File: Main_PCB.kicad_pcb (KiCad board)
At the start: 0 parts

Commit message: added battery holder and swd programming port
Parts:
- added A1: Arduino_UNO_R3, Module:Arduino_UNO_R3, F.Cu at (129.0, 71.5)
- added C3: 4pF, Capacitor_SMD:C_0603_1608Metric_Pad1.08x0.95mm_HandSolder, F.Cu at (96.1, 138.8)
- added C4: 4pF, Capacitor_SMD:C_0603_1608Metric_Pad1.08x0.95mm_HandSolder, F.Cu at (110.6, 124.3)
- added F1: Fuse, Fuse:Fuse_0603_1608Metric_Pad1.05x0.95mm_HandSolder, F.Cu at (208.7, 69.4)
- added JP1: 20021521-00010T1LF, 20021521-00010T1LF:20021521-00010T1LF, F.Cu at (205.5, 144.0)
- added U3: Dual_AA, Dual_AA:Dual_AA, F.Cu at (237.0, 73.5)
- added U4: STM32L476RGTx, Package_QFP:LQFP-64_10x10mm_P0.5mm, F.Cu at (150.5, 95.0)
- added Y1: 32.768, Crystal:Crystal_SMD_3215-2Pin_3.2x1.5mm, F.Cu at (110.9, 136.0)
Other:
- copper layers 0 -> 2

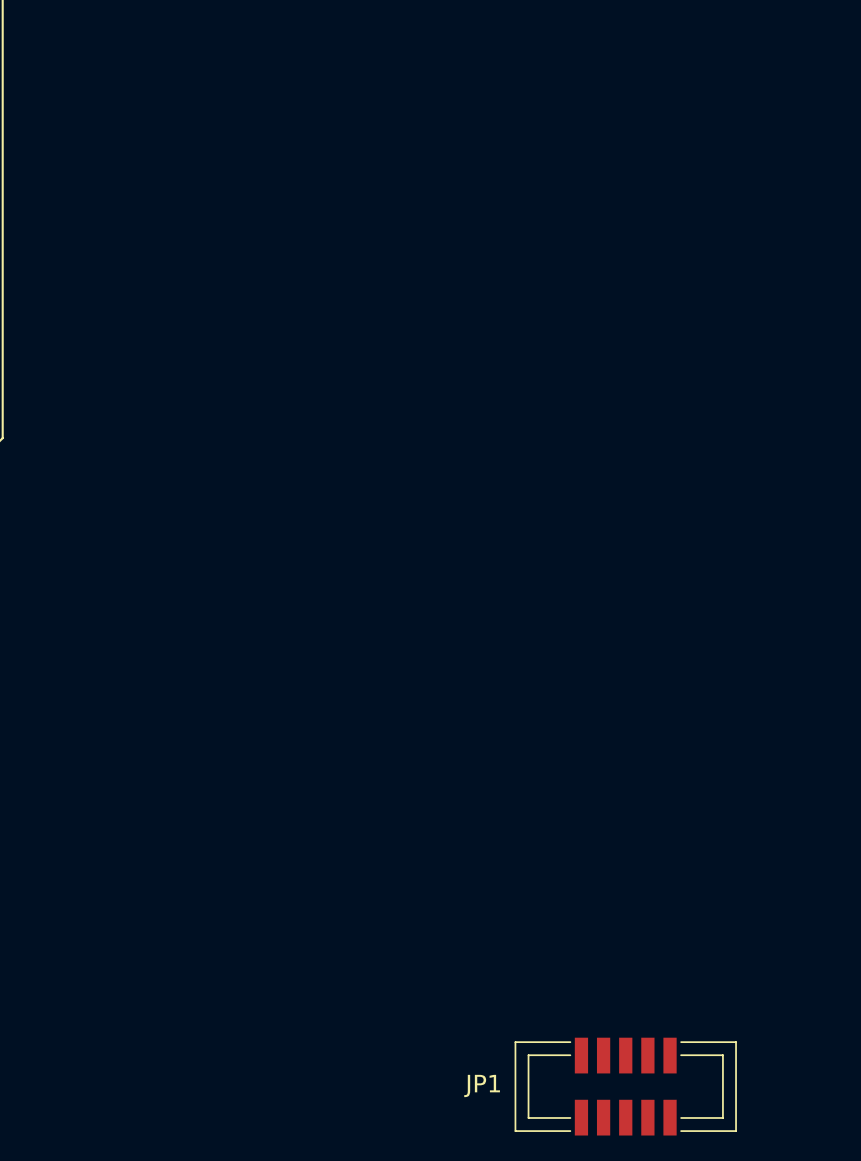
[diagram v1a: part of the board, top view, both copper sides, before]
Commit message: assigned footprints
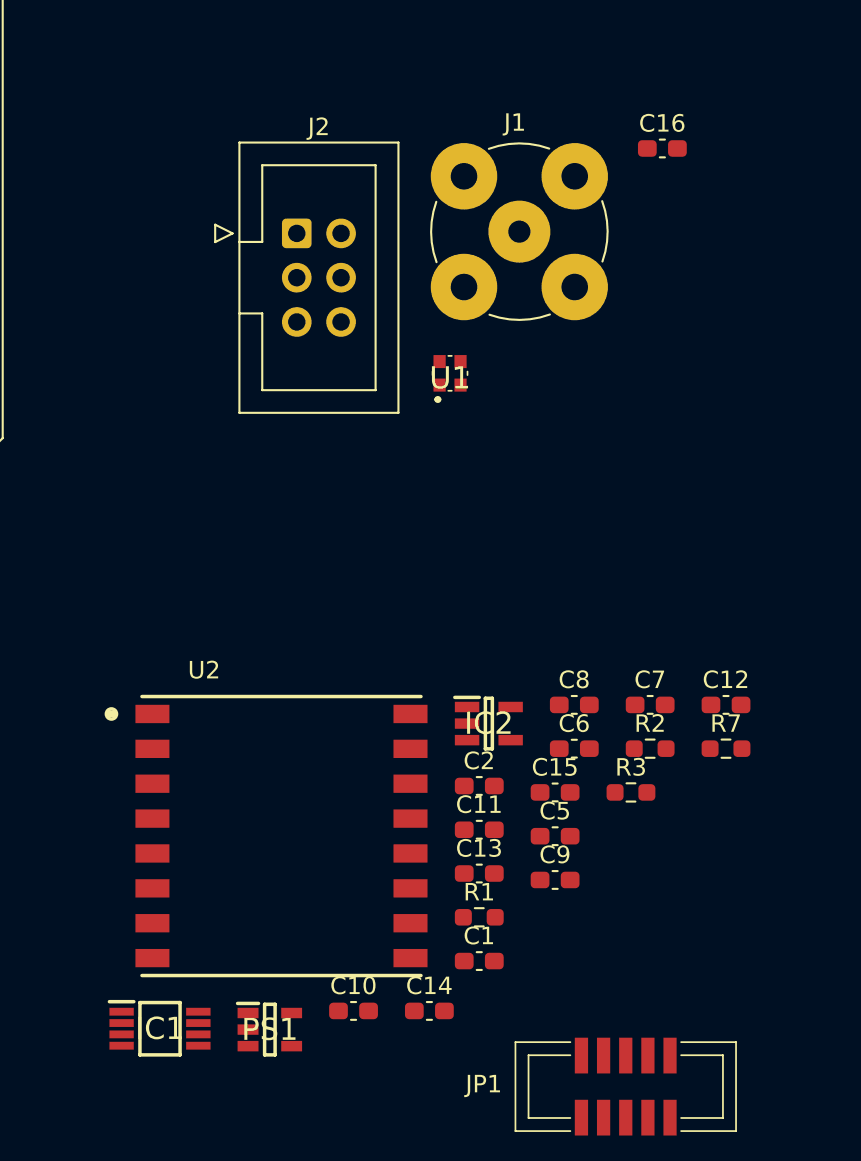
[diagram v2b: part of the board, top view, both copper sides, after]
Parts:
- added C1: 100nF, Capacitor_SMD:C_0603_1608Metric_Pad1.08x0.95mm_HandSolder, F.Cu at (197.1, 136.8)
- added C10: 100nF, Capacitor_SMD:C_0603_1608Metric_Pad1.08x0.95mm_HandSolder, F.Cu at (189.9, 139.7)
- added C11: 100nF, Capacitor_SMD:C_0603_1608Metric_Pad1.08x0.95mm_HandSolder, F.Cu at (197.1, 129.3)
- added C12: 100nF, Capacitor_SMD:C_0603_1608Metric_Pad1.08x0.95mm_HandSolder, F.Cu at (211.2, 122.1)
- added C13: 100nF, Capacitor_SMD:C_0603_1608Metric_Pad1.08x0.95mm_HandSolder, F.Cu at (197.1, 131.8)
- added C14: 100nF, Capacitor_SMD:C_0603_1608Metric_Pad1.08x0.95mm_HandSolder, F.Cu at (194.2, 139.7)
- added C15: 100nF, Capacitor_SMD:C_0603_1608Metric_Pad1.08x0.95mm_HandSolder, F.Cu at (201.4, 127.1)
- added C16: 100nF, Capacitor_SMD:C_0603_1608Metric_Pad1.08x0.95mm_HandSolder, F.Cu at (207.6, 90.2)
- added C2: 100nF, Capacitor_SMD:C_0603_1608Metric_Pad1.08x0.95mm_HandSolder, F.Cu at (197.1, 126.8)
- added C5: 100nF, Capacitor_SMD:C_0603_1608Metric_Pad1.08x0.95mm_HandSolder, F.Cu at (201.4, 129.6)
- added C6: 100nF, Capacitor_SMD:C_0603_1608Metric_Pad1.08x0.95mm_HandSolder, F.Cu at (202.6, 124.6)
- added C7: 100nF, Capacitor_SMD:C_0603_1608Metric_Pad1.08x0.95mm_HandSolder, F.Cu at (206.9, 122.1)
- added C8: 100nF, Capacitor_SMD:C_0603_1608Metric_Pad1.08x0.95mm_HandSolder, F.Cu at (202.6, 122.1)
- added C9: 100nF, Capacitor_SMD:C_0603_1608Metric_Pad1.08x0.95mm_HandSolder, F.Cu at (201.4, 132.2)
- added IC1: TCN75AVUA713-VAO, TCN75AVUA713-VAO:SOP65P490X110-8N, F.Cu at (178.8, 140.7)
- added IC2: 24AA64T-I_OT, 24AA64T-I_OT:SOT95P270X145-5N, F.Cu at (197.7, 123.2)
- added J1: Conn_Coaxial, Connector_Coaxial:BNC_TEConnectivity_1478204_Vertical, F.Cu at (199.4, 95.0)
- added J2: Conn_02x03_Odd_Even, Connector_IDC:IDC-Header_2x03_P2.54mm_Vertical, F.Cu at (186.6, 95.1)
- added PS1: S-1318B33-M5T1U4, S-1318B33:SOT95P275X130-5N, F.Cu at (185.1, 140.7)
- added R1: 0R, Resistor_SMD:R_0603_1608Metric_Pad0.98x0.95mm_HandSolder, F.Cu at (197.1, 134.3)
- added R2: 0R, Resistor_SMD:R_0603_1608Metric_Pad0.98x0.95mm_HandSolder, F.Cu at (206.9, 124.6)
- added R3: 4.7KR, Resistor_SMD:R_0603_1608Metric_Pad0.98x0.95mm_HandSolder, F.Cu at (205.8, 127.1)
- added R7: 10K, Resistor_SMD:R_0603_1608Metric_Pad0.98x0.95mm_HandSolder, F.Cu at (211.2, 124.6)
- added U1: LTR-329ALS-01, LTR-329ALS:LTR329ALS01, F.Cu at (195.4, 103.4)
- added U2: RFM95W-868S2, RFM95W-868S2:XCVR_RFM95W-868S2, F.Cu at (185.8, 129.6)

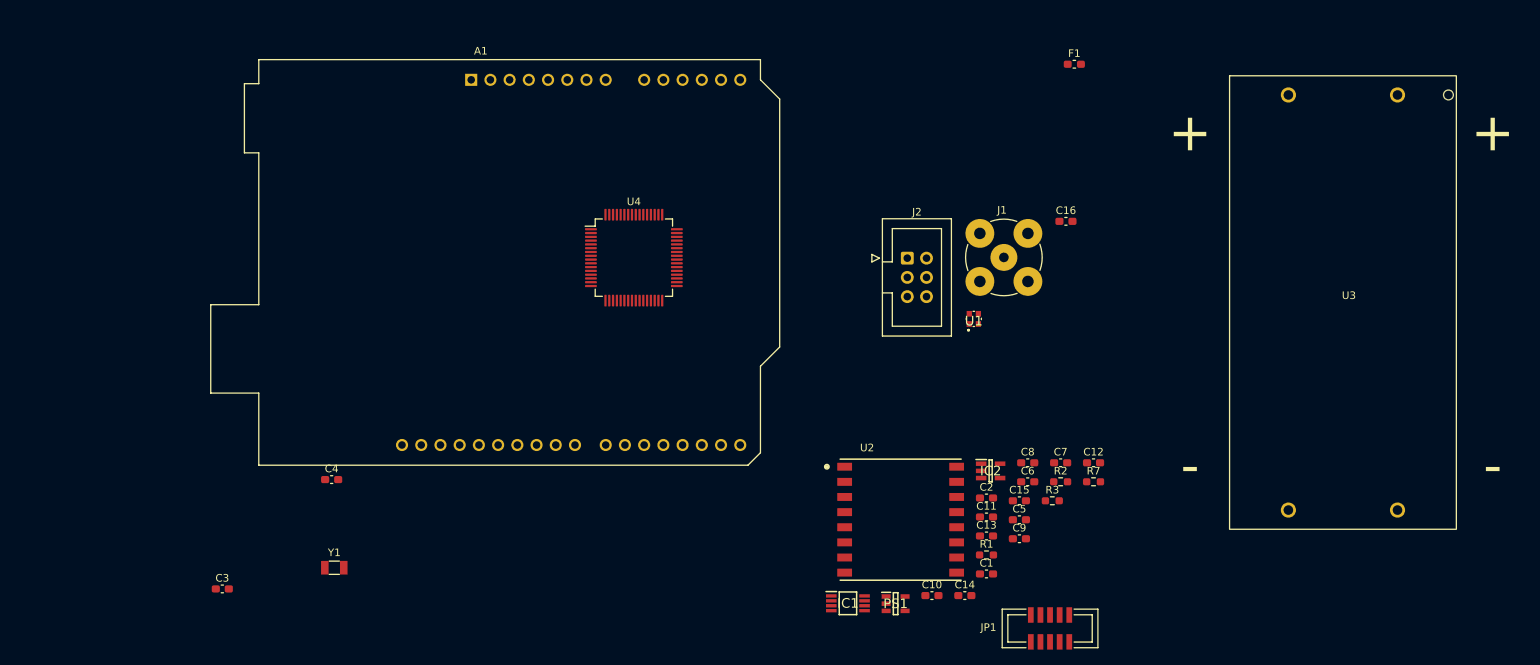
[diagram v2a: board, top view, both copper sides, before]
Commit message: did alot of the routing and pcb layout
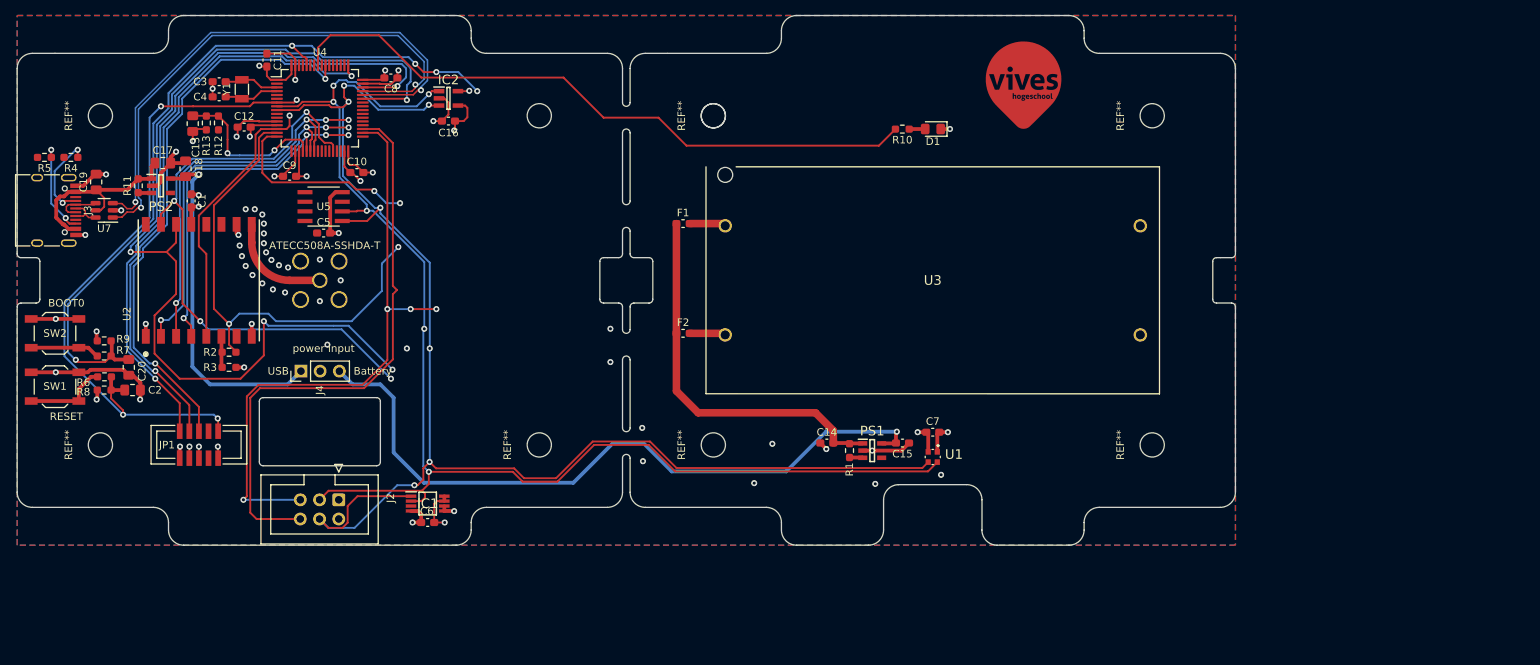
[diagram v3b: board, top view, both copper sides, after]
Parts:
- removed A1: Arduino_UNO_R3, Module:Arduino_UNO_R3
- added ?: , , F.Cu at (161.0, 76.2)
- added C17: 100nF, Capacitor_SMD:C_0805_2012Metric_Pad1.18x1.45mm_HandSolder, F.Cu at (88.2, 82.5)
- added C18: 100nF, Capacitor_SMD:C_0805_2012Metric_Pad1.18x1.45mm_HandSolder, F.Cu at (91.2, 83.2)
- added C19: 100nF, Capacitor_SMD:C_0805_2012Metric_Pad1.18x1.45mm_HandSolder, F.Cu at (79.4, 85.0)
- added C20: 100nF, Capacitor_SMD:C_0805_2012Metric_Pad1.18x1.45mm_HandSolder, F.Cu at (83.8, 109.5)
- added D1: LED, LED_SMD:LED_0805_2012Metric_Pad1.15x1.40mm_HandSolder, F.Cu at (190.0, 78.0)
- added F2: Fuse, Fuse:Fuse_0603_1608Metric_Pad1.05x0.95mm_HandSolder, F.Cu at (157.0, 105.0)
- added G***: LOGO, logo's:VIVES_LOGO_10MM, F.Cu at (202.0, 73.0)
- added J3: USB_C_Receptacle_USB2.0, Connector_USB:USB_C_Receptacle_HRO_TYPE-C-31-M-12, F.Cu at (72.7, 88.8)
- added J4: Conn_01x03_Male, Connector_PinHeader_2.54mm:PinHeader_1x03_P2.54mm_Vertical, F.Cu at (106.5, 110.0)
- added PS2: S-1318B33-M5T1U4, S-1318B33:SOT95P275X130-5N, F.Cu at (88.0, 85.5)
- added R10: 360R, Resistor_SMD:R_0603_1608Metric_Pad0.98x0.95mm_HandSolder, F.Cu at (186.0, 78.0)
- added R11: 0R, Resistor_SMD:R_0603_1608Metric_Pad0.98x0.95mm_HandSolder, F.Cu at (85.0, 85.5)
- added R12: 220k, Resistor_SMD:R_0603_1608Metric_Pad0.98x0.95mm_HandSolder, F.Cu at (95.6, 77.2)
- added R13: 330k, Resistor_SMD:R_0603_1608Metric_Pad0.98x0.95mm_HandSolder, F.Cu at (94.0, 77.2)
- added R4: 5.1k, Resistor_SMD:R_0603_1608Metric_Pad0.98x0.95mm_HandSolder, F.Cu at (76.1, 81.8)
- added R5: 5.1k, Resistor_SMD:R_0603_1608Metric_Pad0.98x0.95mm_HandSolder, F.Cu at (72.6, 81.8)
- added R6: 360R, Resistor_SMD:R_0603_1608Metric_Pad0.98x0.95mm_HandSolder, F.Cu at (80.5, 110.8)
- added R8: 100k, Resistor_SMD:R_0603_1608Metric_Pad0.98x0.95mm_HandSolder, F.Cu at (80.5, 112.5)
- added R9: 100k, Resistor_SMD:R_0603_1608Metric_Pad0.98x0.95mm_HandSolder, F.Cu at (80.5, 106.0)
- added REF**: MountingHole_3.2mm_M3, MountingHole:MountingHole_3.2mm_M3, F.Cu at (80.0, 119.8)
- added REF**: MountingHole_3.2mm_M3, MountingHole:MountingHole_3.2mm_M3, F.Cu at (219.0, 119.8)
- added REF**: MountingHole_3.2mm_M3, MountingHole:MountingHole_3.2mm_M3, F.Cu at (161.0, 76.2)
- added REF**: MountingHole_3.2mm_M3, MountingHole:MountingHole_3.2mm_M3, F.Cu at (138.0, 119.8)
- added REF**: MountingHole_3.2mm_M3, MountingHole:MountingHole_3.2mm_M3, F.Cu at (161.0, 119.8)
- added REF**: MountingHole_3.2mm_M3, MountingHole:MountingHole_3.2mm_M3, F.Cu at (80.0, 76.2)
- added REF**: MountingHole_3.2mm_M3, MountingHole:MountingHole_3.2mm_M3, F.Cu at (138.0, 76.2)
- added REF**: MountingHole_3.2mm_M3, MountingHole:MountingHole_3.2mm_M3, F.Cu at (219.0, 76.2)
- added SW1: SW_Push, Button_Switch_SMD:SW_SPST_TL3342, F.Cu at (74.0, 112.0)
- added SW2: SW_Push, Button_Switch_SMD:SW_SPST_TL3342, F.Cu at (74.0, 105.0)
- added U5: ATECC508A-SSHDA-T, ATECC508A:ATECC508A-SSHDA-T, F.Cu at (109.5, 88.2)
- added U7: USBLC6-2SC6, Package_TO_SOT_SMD:SOT-23-6, F.Cu at (80.5, 88.8)
- C13, C2: footprint Capacitor_SMD:C_0603_1608Metric_Pad1.08x0.95mm_HandSolder -> Capacitor_SMD:C_0805_2012Metric_Pad1.18x1.45mm_HandSolder
- J1: footprint Connector_Coaxial:BNC_TEConnectivity_1478204_Vertical -> Connector_Coaxial:SMA_Amphenol_901-144_Vertical; moved to B.Cu
- R7: value 10K -> 360R
- U3: value Dual_AA -> 1013; footprint Dual_AA:Dual_AA -> 1013:1013
- moved R7 131.8 mm to (80.5, 108.0)
- moved C12 120.7 mm to (99.0, 77.8)
- moved C13 118.2 mm to (92.2, 77.3), turned to -90 degrees
- moved C1 116.1 mm to (92.0, 87.5), turned to -90 degrees
- moved JP1 115.1 mm to (93.0, 119.7)
- moved C2 113.7 mm to (84.2, 112.5)
- moved C11 112.7 mm to (102.0, 68.9), turned to -90 degrees
- moved R2 111.2 mm to (97.0, 107.5)
- moved R3 110.2 mm to (97.0, 109.5), turned to 180 degrees
- moved C9 107.7 mm to (105.0, 84.2)
- moved C5 99.5 mm to (109.5, 91.8)
- moved C8 98.3 mm to (118.4, 71.2), turned to 180 degrees
- moved U2 98.0 mm to (93.0, 98.0), turned to 90 degrees
- moved C10 94.4 mm to (113.9, 83.8)
- moved J1 90.5 mm to (109.0, 98.0)
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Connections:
- C13 pad 1: GND -> /bat_voltage
- C13 pad 2: VCC -> GND
- C15 pad 2: VCC -> /battery
- C2 pad 1: GND -> /Reset
- C2 pad 2: VCC -> GND
- IC2 pad 1: /I2C_EEPROM_SCL -> /IC2_MoistureSensor_SCL1
- IC2 pad 3: /I2C_EEPROM_SDA -> /IC2_MoistureSensor_SDA1
- IC2 pad 5: unconnected-(IC2-Pad5) -> GND
- PS1 pad 5: VCC -> /battery
- R7 pad 2: GND -> /boot0
- U3 pad 2: Net-(F1-Pad2) -> Net-(F2-Pad2)
- U4 pad 10: unconnected-(U4-Pad10) -> /PC2
- U4 pad 11: unconnected-(U4-Pad11) -> /PC3
- U4 pad 2: unconnected-(U4-Pad2) -> /PC13
- U4 pad 20: /A2 -> /bat_voltage
- U4 pad 24: unconnected-(U4-Pad24) -> /PC4
- U4 pad 25: unconnected-(U4-Pad25) -> /PC5
- U4 pad 27: unconnected-(U4-Pad27) -> /PB1
- U4 pad 30: unconnected-(U4-Pad30) -> /PB11
- U4 pad 33: unconnected-(U4-Pad33) -> /PB12
- U4 pad 36: unconnected-(U4-Pad36) -> /PB15
- U4 pad 37: unconnected-(U4-Pad37) -> /PC6
- U4 pad 39: unconnected-(U4-Pad39) -> /PC8
- U4 pad 40: unconnected-(U4-Pad40) -> /PC9
- U4 pad 44: unconnected-(U4-Pad44) -> USB-
- U4 pad 45: unconnected-(U4-Pad45) -> USB+
- U4 pad 5: unconnected-(U4-Pad5) -> /PH0
- U4 pad 50: unconnected-(U4-Pad50) -> /PA15
- U4 pad 51: unconnected-(U4-Pad51) -> /PC10
- U4 pad 52: unconnected-(U4-Pad52) -> /PC11
- U4 pad 53: unconnected-(U4-Pad53) -> /PC12
- U4 pad 54: unconnected-(U4-Pad54) -> /PD2
- U4 pad 59: /I2C_EEPROM_SDA -> /PB7
- U4 pad 6: unconnected-(U4-Pad6) -> /PH1
- U4 pad 60: Net-(R7-Pad1) -> /boot0
- U4 pad 61: /I2C_EEPROM_SCL -> /PB8
- U4 pad 62: unconnected-(U4-Pad62) -> /PB9
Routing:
- net /IC2_MoistureSensor_SDA1: track 0.00 -> 191.3 mm, vias 0 -> 7
- net /IC2_MoistureSensor_SCL1: track 0.00 -> 176.1 mm, vias 0 -> 6
- net /LORA_DIO0: track 0.00 -> 133.7 mm, vias 0 -> 4
- net GND: track 0.00 -> 110.4 mm, vias 0 -> 59
- net /boot0: track 0.00 -> 100.2 mm, vias 0 -> 5
- net /battery: track 0.00 -> 93.4 mm, vias 0 -> 1
- net /SWDIO: track 0.00 -> 91.0 mm, vias 0 -> 2
- net /Reset: track 0.00 -> 89.4 mm, vias 0 -> 4
- net /D4: track 0.00 -> 86.3 mm
- net /LORA_DIO1: track 0.00 -> 82.0 mm, vias 0 -> 4
- net /IC2_MoistureSensor_SCL2: track 0.00 -> 80.9 mm, vias 0 -> 4
- net /SWCLK: track 0.00 -> 78.0 mm, vias 0 -> 2
- net /IC2_MoistureSensor_SDA2: track 0.00 -> 76.9 mm
- net /SWO: track 0.00 -> 74.5 mm, vias 0 -> 2
- net USB-: track 0.00 -> 72.9 mm, vias 0 -> 2
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- added copper zone on B.Cu, net GND
- added copper zone on F.Cu, net GND
- added copper zone on In2.Cu, net GND
- added copper zone on In1.Cu, net VCC
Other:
- board outline added: 161 x 70 mm
- copper layers 2 -> 4
- board text added: "BOOT0"
- board text added: "Battery"
- board text added: "RESET"
- board text added: "USB"
- board text added: "power input"

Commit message: added some 3d files and pcb updates
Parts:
- moved C5 0.50 mm to (109.0, 91.8)
- moved U5 0.50 mm to (109.0, 88.2)
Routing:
- net VBAT: track 50.6 -> 156.5 mm, vias 0 -> 2
- net Lora-Reset: track 64.2 -> 34.7 mm, vias 2 -> 0
- net /D1_TX: track 26.2 -> 0.00 mm, vias 2 -> 0
- net /IC2_MoistureSensor_SCL2: track 80.9 -> 74.5 mm, vias 4 -> 1
- net /IC2_MoistureSensor_SCL1: track 176.1 -> 177.8 mm, vias 6 -> 5
- net /IC2_MoistureSensor_SDA1: track 191.3 -> 192.6 mm, vias 7 -> 6
- net /battery: track 93.4 -> 94.0 mm
